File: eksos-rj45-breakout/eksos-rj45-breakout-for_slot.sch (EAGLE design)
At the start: 6 parts, among them X1 RJ45-8X-DS1130, X2 RJ45-8X-DS1130

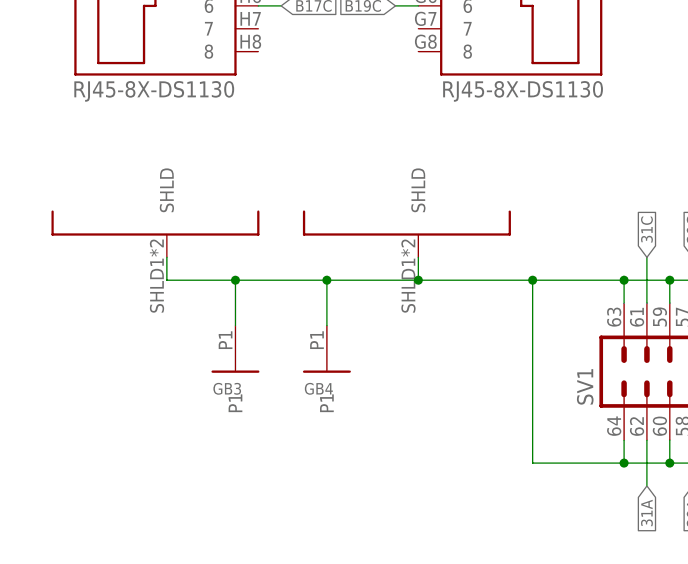
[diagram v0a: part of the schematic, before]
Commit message: eksos-rj45-breakout: Update DS1130 library (3 more SHLD, 1 more drill)
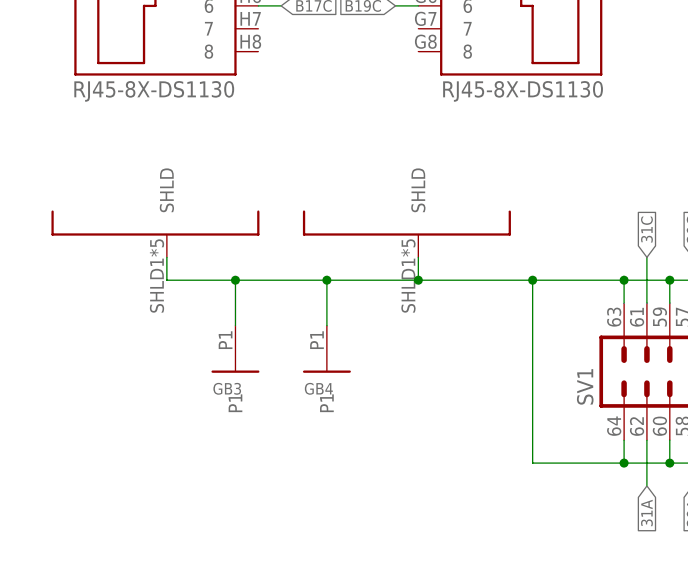
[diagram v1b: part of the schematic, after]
